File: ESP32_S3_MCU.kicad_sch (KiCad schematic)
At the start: 30 parts, among them SW1 SW_Push, SW2 SW_Push, U1 W25Q32JVSS, U2 ESP32-C3, X1 40MHz

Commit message: Update placement
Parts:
- removed C2: 10u, Capacitor_SMD:C_1210_3225Metric, symbol Device:C_Small
- removed C3, C4, C5, C6: 100n, Capacitor_SMD:C_0603_1608Metric, symbol Device:C_Small
- removed C8: 10u, Capacitor_SMD:C_0603_1608Metric, symbol Device:C_Small
- removed R2, R8: 470R, Resistor_SMD:R_0402_1005Metric, symbol Device:R_Small
- removed R3: 22R, Resistor_SMD:R_0402_1005Metric, symbol Device:R_Small
- removed U2: ESP32-C3, Package_DFN_QFN:QFN-32-1EP_5x5mm_P0.5mm_EP3.45x3.45mm, symbol PCM_Espressif:ESP32-C3
- added C33: 10nF, Capacitor_SMD:C_0402_1005Metric, symbol Device:C_Small
- added C34: 1uF, Capacitor_SMD:C_0402_1005Metric, symbol Device:C_Small
- added C6 (x3), C8: 100n, Capacitor_SMD:C_0402_1005Metric, symbol Device:C_Small
- added C8: 10u, Capacitor_SMD:C_0603_1608Metric, symbol Device:C_Small
- added C8 (x2): 1u, Capacitor_SMD:C_0402_1005Metric, symbol Device:C_Small
- added U8: ESP32-S3, Package_DFN_QFN:QFN-56-1EP_7x7mm_P0.4mm_EP5.6x5.6mm, symbol PCM_Espressif:ESP32-S3
- C1, C11, C12, C21, C22, C7: footprint Capacitor_SMD:C_0603_1608Metric -> Capacitor_SMD:C_0402_1005Metric
- C10, C9: value 10p -> 20p
- L1: footprint Inductor_SMD:L_0603_1608Metric -> Inductor_SMD:L_0402_1005Metric
- U5: footprint RF_Antenna:Texas_SWRA117D_2.4GHz_Right -> RF_Antenna:Texas_SWRA117D_2.4GHz_Left
- X1: footprint Crystal:Crystal_SMD_2520-4Pin_2.5x2.0mm -> KiCADv7:OSC_X322516MLB4SI; Field5 C255973 -> (none); LCSC (none) -> C13738
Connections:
- net +3V3: now also C33.1, C34.1, C6.1, C6.1, C8.1, C8.1, U8.20 (VDD3P3_RTC), U8.46 (VDD3P3_CPU), U8.55 (VDDA), U8.56 (VDDA)
- net CHIP_EN: now also U8.4 (CHIP_PU/RESET)
- net FSPI_CLK: now also U8.44 (MTCK/JTAG/GPIO39)
- net FSPI_D: now also U8.45 (MTDO/JTAG/GPIO40)
- net FSPI_NCS: now also U8.23 (GPIO17/ADC2_CH6)
- net FSPI_NCS2: now also U8.19 (GPIO14/ADC2_CH3)
- net FSPI_Q: now also U8.18 (GPIO13/ADC2_CH2)
- net GND: now also C33.2, C34.2, C6.2, C6.2, C6.2, C8.2, C8.2, C8.2, C8.2, U8.57 (GND)
- net INT_ACC: now also U8.17 (GPIO12/ADC2_CH1)
- net INT_GYR_GPIO9: now also U8.16 (GPIO11/ADC2_CH0); no longer C1.1, R1.2, SW2.2
- net MOTOR_1_DIRECTION: now also U8.7 (GPIO2/ADC1_CH1)
- net MOTOR_1_PWM: now also U8.6 (GPIO1/ADC1_CH0)
- net MOTOR_2_DIRECTION: now also U8.9 (GPIO4/ADC1_CH3)
- net MOTOR_2_PWM: now also U8.8 (GPIO3/ADC1_CH2)
- net RF: now also U8.1 (LNA_IN/RF)
- net SPICLK: now also U8.33 (SPICLK/GPIO30)
- net SPICSO: now also U8.32 (SPICS0/GPIO29)
- net SPID: now also R11.1, U8.35 (SPID/GPIO32)
- net SPIHD: now also U8.30 (SPIHD/GPIO27)
- net SPIQ: now also U8.34 (SPIQ/GPIO31); no longer R11.1
- net SPIWP: now also U8.31 (SPIWP/GPIO28)
- net USB_D_N: now also U8.25 (GPIO19/USB_D-/ADC2_CH8)
- net USB_D_P: now also U8.26 (GPIO20/USB_D+/ADC2_CH9)
- net VDD_SPI: now also C8.1, C8.1, U8.29 (VDD_SPI)
- net V_RF: now also C6.1, U8.2 (VDD3P3), U8.3 (VDD3P3)
- net at C9.1, X1.3: now also U8.53 (XTAL_N)
- net at C10.1, X1.1: now also U8.54 (XTAL_P)
- new net CHIP_BOOT: C1.1, R1.2, SW2.2, U8.5 (GPIO0/BOOT)
- new net MOTOR_3_DIRECTION: U8.11 (GPIO6/ADC1_CH5)
- new net MOTOR_3_PWM: U8.10 (GPIO5/ADC1_CH4)
- new net MOTOR_4_DIRECTION: U8.13 (GPIO8/ADC1_CH7)
- new net MOTOR_4_PWM: U8.12 (GPIO7/ADC1_CH6)
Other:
- moved on the sheet: C12, C13, C21, C22, L1, U1, U5

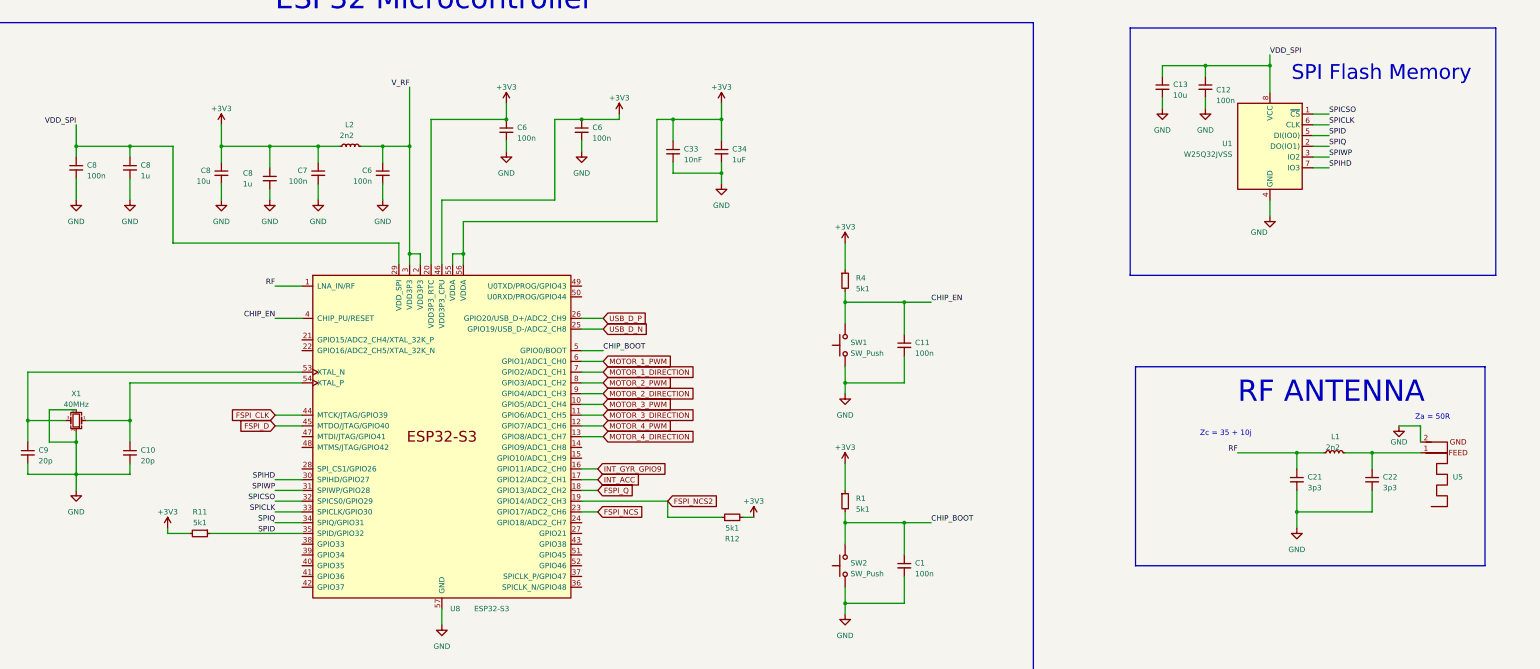
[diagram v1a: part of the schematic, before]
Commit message: route usb and flash
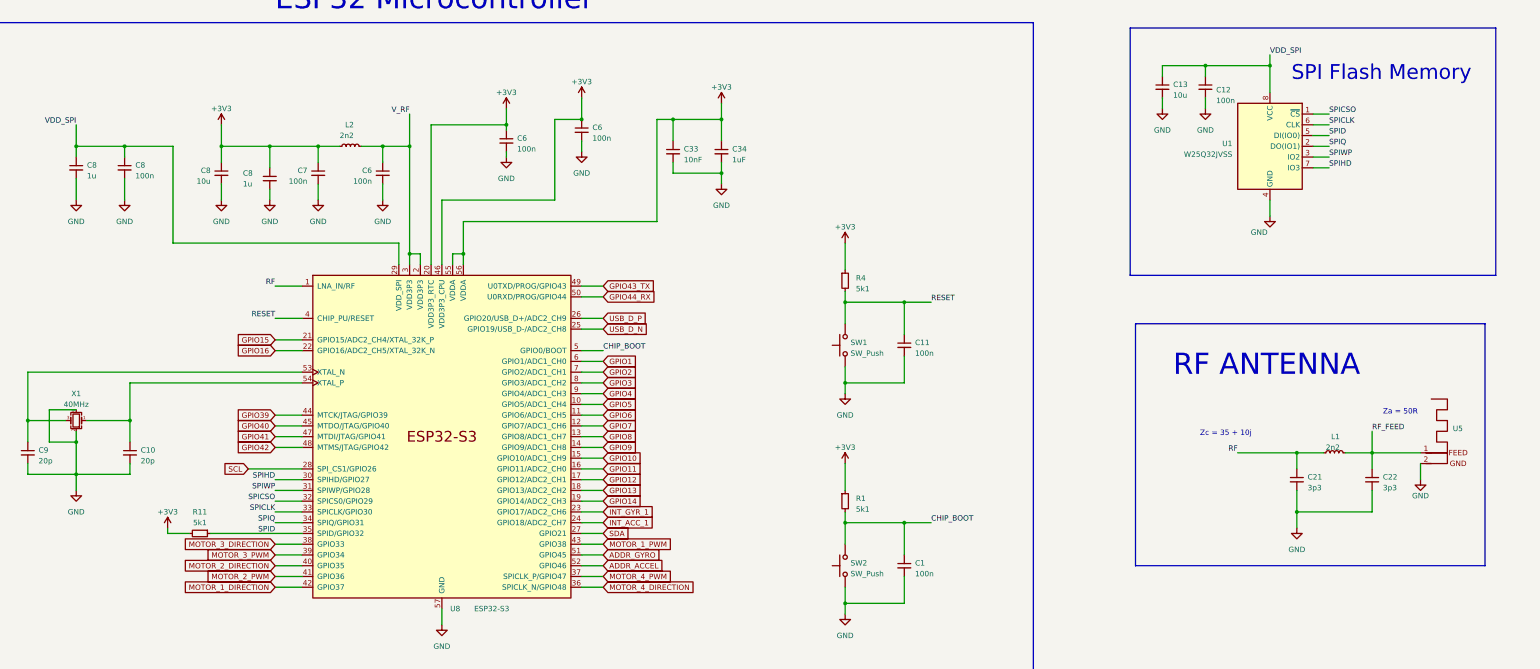
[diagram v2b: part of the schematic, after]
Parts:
- removed R12: 5k1, Resistor_SMD:R_0603_1608Metric, symbol Device:R_Small
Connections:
- net MOTOR_1_DIRECTION: now also U8.42 (GPIO37); no longer U8.7 (GPIO2/ADC1_CH1)
- net MOTOR_1_PWM: now also U8.43 (GPIO38); no longer U8.6 (GPIO1/ADC1_CH0)
- net MOTOR_2_DIRECTION: now also U8.40 (GPIO35); no longer U8.9 (GPIO4/ADC1_CH3)
- net MOTOR_2_PWM: now also U8.41 (GPIO36); no longer U8.8 (GPIO3/ADC1_CH2)
- net MOTOR_3_DIRECTION: now also U8.38 (GPIO33); no longer U8.11 (GPIO6/ADC1_CH5)
- net MOTOR_3_PWM: now also U8.39 (GPIO34); no longer U8.10 (GPIO5/ADC1_CH4)
- net MOTOR_4_DIRECTION: now also U8.36 (SPICLK_N/GPIO48); no longer U8.13 (GPIO8/ADC1_CH7)
- net MOTOR_4_PWM: now also U8.37 (SPICLK_P/GPIO47); no longer U8.12 (GPIO7/ADC1_CH6)
- net RF_FEED: now reaches C22.1, L1.2, U5.1
- net GPIO9: now reaches U8.14 (GPIO9/ADC1_CH8)
- net GPIO10: now reaches U8.15 (GPIO10/ADC1_CH9)
- net GPIO15: now reaches U8.21 (GPIO15/ADC2_CH4/XTAL_32K_P)
- net GPIO16: now reaches U8.22 (GPIO16/ADC2_CH5/XTAL_32K_N)
- net INT_ACC_1: now reaches U8.24 (GPIO18/ADC2_CH7)
- net SDA: now reaches U8.27 (GPIO21)
- net SCL: now reaches U8.28 (SPI_CS1/GPIO26)
- net GPIO41: now reaches U8.47 (MTDI/JTAG/GPIO41)
- net GPIO42: now reaches U8.48 (MTMS/JTAG/GPIO42)
- net GPIO43_TX: now reaches U8.49 (U0TXD/PROG/GPIO43)
- net GPIO44_RX: now reaches U8.50 (U0RXD/PROG/GPIO44)
- net ADDR_GYRO: now reaches U8.51 (GPIO45)
- net ADDR_ACCEL: now reaches U8.52 (GPIO46)
- net CHIP_EN renamed RESET
- net FSPI_CLK renamed GPIO39
- net FSPI_D renamed GPIO40
- net FSPI_NCS renamed INT_GYR_1
- net FSPI_NCS2 renamed GPIO14
- net FSPI_Q renamed GPIO13
- net INT_ACC renamed GPIO12
- net INT_GYR_GPIO9 renamed GPIO11
- new net GPIO1: U8.6 (GPIO1/ADC1_CH0)
- new net GPIO2: U8.7 (GPIO2/ADC1_CH1)
- new net GPIO3: U8.8 (GPIO3/ADC1_CH2)
- new net GPIO4: U8.9 (GPIO4/ADC1_CH3)
- new net GPIO5: U8.10 (GPIO5/ADC1_CH4)
- new net GPIO6: U8.11 (GPIO6/ADC1_CH5)
- new net GPIO7: U8.12 (GPIO7/ADC1_CH6)
- new net GPIO8: U8.13 (GPIO8/ADC1_CH7)
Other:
- moved on the sheet: C6, C8, U5

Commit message: route motors
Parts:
- renumbered C11 to C15, C1 to C16, C13 to C19, C12 to C20, C9 to C23, C8 to C24, C8 to C25, C10 to C26, C8 to C27, C8 to C28, C7 to C29, C6 to C30, C6 to C31, C6 to C32, L1 to L2, L2 to L3, R1 to R10, R11 to R12, R4 to R8, SW1 to SW2, SW2 to SW4, U1 to U6, U5 to U7, X1 to X2

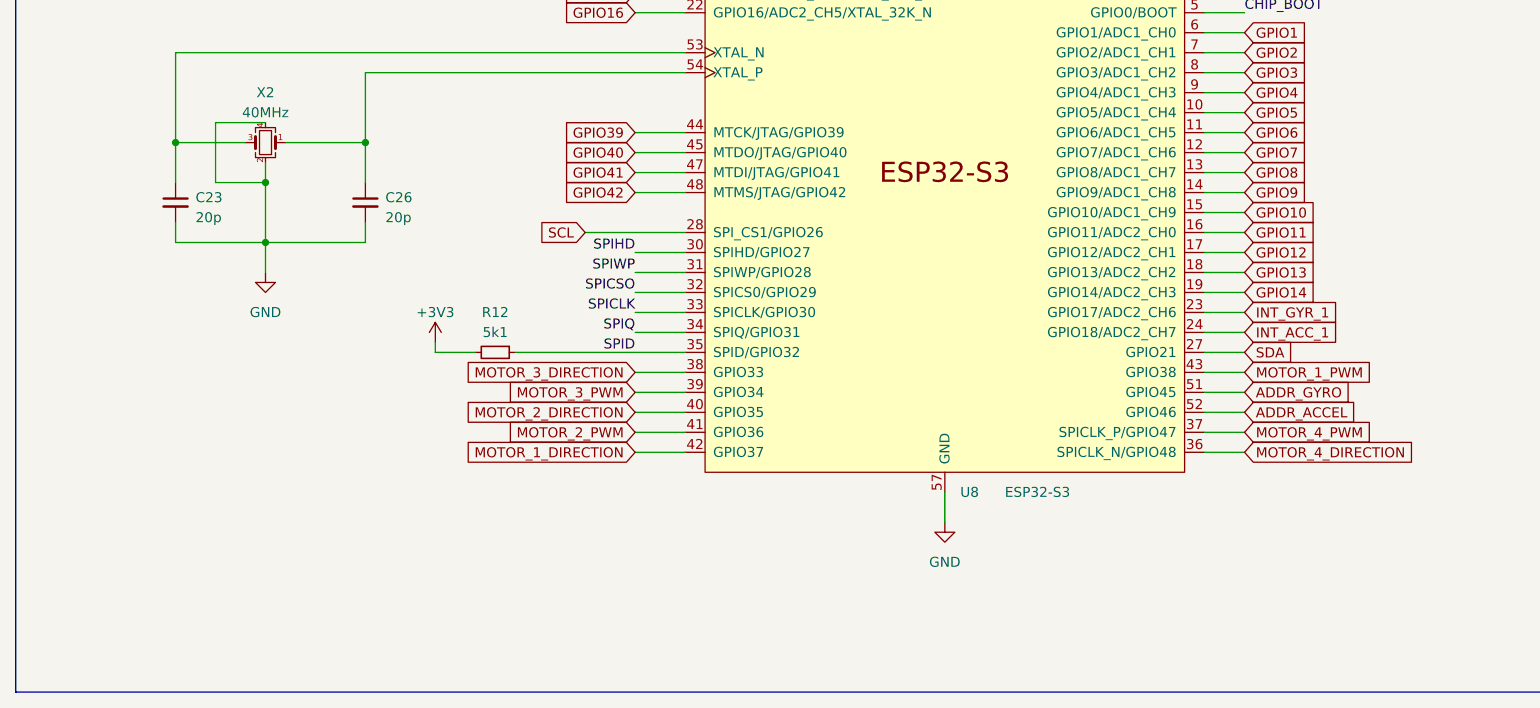
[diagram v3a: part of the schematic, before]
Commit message: Add MPU6050 and LIS2MDL
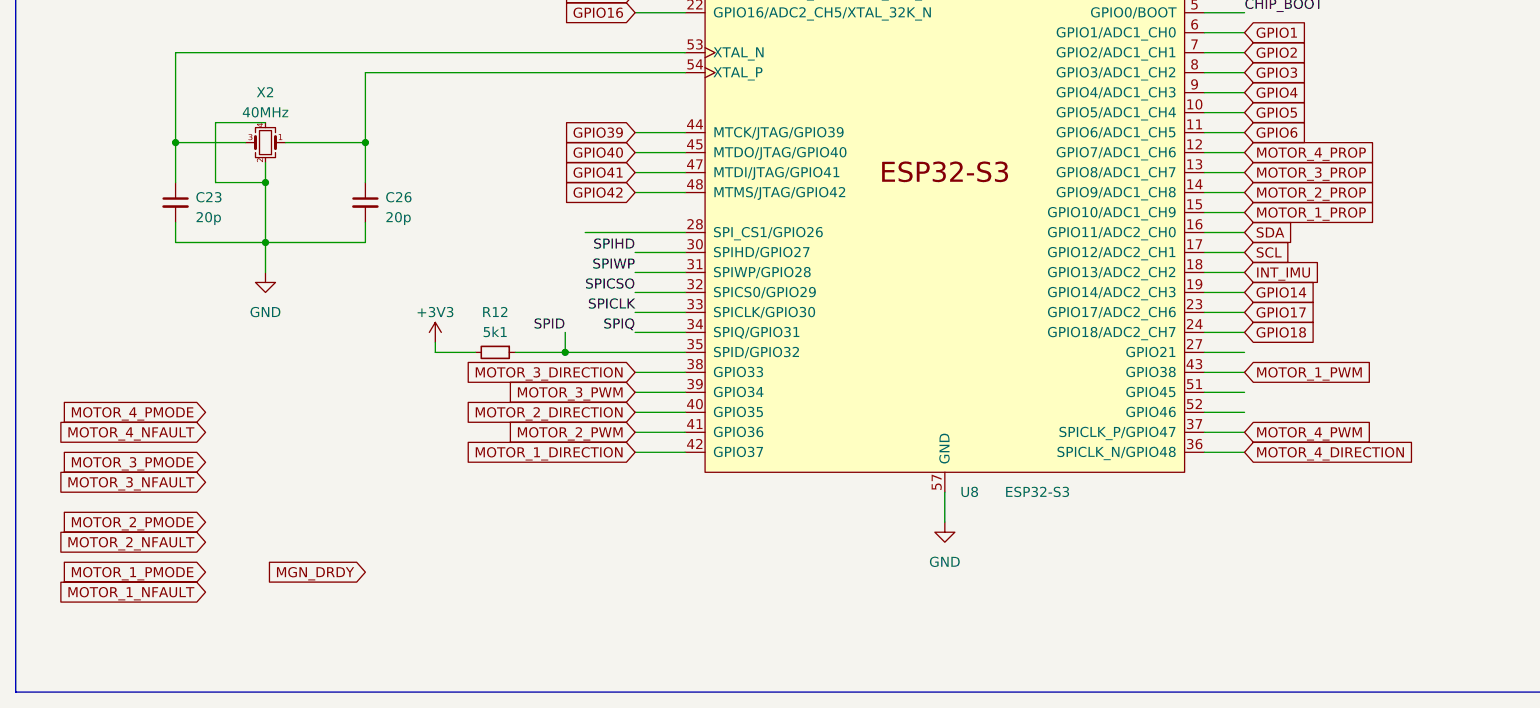
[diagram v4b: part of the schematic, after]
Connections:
- net GPIO11 is gone; now on net SDA: U8.16 (GPIO11/ADC2_CH0)
- net GPIO12 is gone; now on net SCL: U8.17 (GPIO12/ADC2_CH1)
- net SCL: no longer U8.28 (SPI_CS1/GPIO26)
- net SDA: no longer U8.27 (GPIO21)
- net ADDR_ACCEL: no longer names the net of U8.52 (GPIO46)
- net ADDR_GYRO: no longer names the net of U8.51 (GPIO45)
- net GPIO10 renamed MOTOR_1_PROP
- net GPIO13 renamed INT_IMU
- net GPIO7 renamed MOTOR_4_PROP
- net GPIO8 renamed MOTOR_3_PROP
- net GPIO9 renamed MOTOR_2_PROP
- net INT_ACC_1 renamed GPIO18
- net INT_GYR_1 renamed GPIO17

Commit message: checkpoint for backup
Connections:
- net MOTOR_NFAULT: now reaches U8.27 (GPIO21)
- net GPIO26: now reaches U8.28 (SPI_CS1/GPIO26)
- net GPIO45: now reaches U8.51 (GPIO45)
- net GPIO46: now reaches U8.52 (GPIO46)
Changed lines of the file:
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@@
     (stroke (width 0) (type default))
   )
-  (wire (pts (xy 97.79 158.75) (xy 110.49 158.75))
+  (wire (pts (xy 104.14 158.75) (xy 110.49 158.75))
     (stroke (width 0) (type default))
   )
@@
   )
   (wire (pts (xy 194.31 100.33) (xy 194.31 76.2))
+    (stroke (width 0) (type default))
+  )
+  (wire (pts (xy 104.14 157.48) (xy 104.14 158.75))
     (stroke (width 0) (type default))
   )
@@
     )
   )
-  (global_label "MOTOR_4_NFAULT" (shape input) (at 49.53 184.15 180) (fields_autoplaced)
-    (effects (font (size 1.27 1.27)) (justify right))
-    (property "Intersheetrefs" "${INTERSHEET_REFS}" (at 30.2162 184.15 0)
-      (effects (font (size 1.27 1.27)) (justify right) hide)
-    )
-  )
-  (global_label "MOTOR_1_NFAULT" (shape input) (at 49.53 204.47 180) (fields_autoplaced)
-    (effects (font (size 1.27 1.27)) (justify right))
-    (property "Intersheetrefs" "${INTERSHEET_REFS}" (at 30.2162 204.47 0)
-      (effects (font (size 1.27 1.27)) (justify right) hide)
+  (global_label "MOTOR_NFAULT" (shape input) (at 181.61 173.99 0) (fields_autoplaced)
+    (effects (font (size 1.27 1.27)) (justify left))
+    (property "Intersheetrefs" "${INTERSHEET_REFS}" (at 198.7467 173.99 0)
+      (effects (font (size 1.27 1.27)) (justify left) hide)
     )
   )
@@
     )
   )
-  (global_label "MOTOR_2_NFAULT" (shape input) (at 49.53 198.12 180) (fields_autoplaced)
-    (effects (font (size 1.27 1.27)) (justify right))
-    (property "Intersheetrefs" "${INTERSHEET_REFS}" (at 30.2162 198.12 0)
-      (effects (font (size 1.27 1.27)) (justify right) hide)
-    )
-  )
   (global_label "GPIO3" (shape input) (at 181.61 138.43 0) (fields_autoplaced)
     (effects (font (size 1.27 1.27)) (justify left))
@@
     )
   )
+  (global_label "GPIO26" (shape input) (at 104.14 157.48 180) (fields_autoplaced)
+    (effects (font (size 1.27 1.27)) (justify right))
+    (property "Intersheetrefs" "${INTERSHEET_REFS}" (at 94.2605 157.48 0)
+      (effects (font (size 1.27 1.27)) (justify right) hide)
+    )
+  )
   (global_label "MOTOR_2_DIRECTION" (shape input) (at 104.14 181.61 180) (fields_autoplaced)
     (effects (font (size 1.27 1.27)) (justify right))
@@
     )
   )
-  (global_label "MOTOR_2_PMODE" (shape input) (at 49.53 195.58 180) (fields_autoplaced)
-    (effects (font (size 1.27 1.27)) (justify right))
-    (property "Intersheetrefs" "${INTERSHEET_REFS}" (at 30.5792 195.58 0)
-      (effects (font (size 1.27 1.27)) (justify right) hide)
+  (global_label "GPIO46" (shape input) (at 181.61 181.61 0) (fields_autoplaced)
+    (effects (font (size 1.27 1.27)) (justify left))
+    (property "Intersheetrefs" "${INTERSHEET_REFS}" (at 191.4895 181.61 0)
+      (effects (font (size 1.27 1.27)) (justify left) hide)
     )
   )
@@
     )
   )
-  (global_label "MOTOR_1_PMODE" (shape input) (at 49.53 201.93 180) (fields_autoplaced)
-    (effects (font (size 1.27 1.27)) (justify right))
-    (property "Intersheetrefs" "${INTERSHEET_REFS}" (at 30.5792 201.93 0)
-      (effects (font (size 1.27 1.27)) (justify right) hide)
-    )
-  )
-  (global_label "MOTOR_3_NFAULT" (shape input) (at 49.53 190.5 180) (fields_autoplaced)
-    (effects (font (size 1.27 1.27)) (justify right))
-    (property "Intersheetrefs" "${INTERSHEET_REFS}" (at 30.2162 190.5 0)
-      (effects (font (size 1.27 1.27)) (justify right) hide)
-    )
-  )
   (global_label "MOTOR_4_DIRECTION" (shape input) (at 181.61 186.69 0) (fields_autoplaced)
     (effects (font (size 1.27 1.27)) (justify left))
@@
     )
   )
+  (global_label "GPIO45" (shape input) (at 181.61 179.07 0) (fields_autoplaced)
+    (effects (font (size 1.27 1.27)) (justify left))
+    (property "Intersheetrefs" "${INTERSHEET_REFS}" (at 191.4895 179.07 0)
+      (effects (font (size 1.27 1.27)) (justify left) hide)
+    )
+  )
   (global_label "GPIO1" (shape input) (at 181.61 133.35 0) (fields_autoplaced)
     (effects (font (size 1.27 1.27)) (justify left))
@@
     )
   )
-  (global_label "MOTOR_4_PMODE" (shape input) (at 49.53 181.61 180) (fields_autoplaced)
-    (effects (font (size 1.27 1.27)) (justify right))
-    (property "Intersheetrefs" "${INTERSHEET_REFS}" (at 30.5792 181.61 0)
-      (effects (font (size 1.27 1.27)) (justify right) hide)
-    )
-  )
-  (global_label "MOTOR_3_PMODE" (shape input) (at 49.53 187.96 180) (fields_autoplaced)
-    (effects (font (size 1.27 1.27)) (justify right))
-    (property "Intersheetrefs" "${INTERSHEET_REFS}" (at 30.5792 187.96 0)
-      (effects (font (size 1.27 1.27)) (justify right) hide)
-    )
-  )
   (global_label "GPIO40" (shape input) (at 104.14 148.59 180) (fields_autoplaced)
     (effects (font (size 1.27 1.27)) (justify right))
@@
     )
   )
-  (global_label "MGN_DRDY" (shape input) (at 69.85 201.93 180) (fields_autoplaced)
-    (effects (font (size 1.27 1.27)) (justify right))
-    (property "Intersheetrefs" "${INTERSHEET_REFS}" (at 56.9467 201.93 0)
-      (effects (font (size 1.27 1.27)) (justify right) hide)
-    )
-  )

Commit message: Checkpoint before updating MCU
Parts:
- added C10, C54, C57, C9: 100n, Capacitor_SMD:C_0402_1005Metric, symbol Device:C_Small
- added C53: 1u, Capacitor_SMD:C_0402_1005Metric, symbol Device:C_Small
- added C55, C56: 12p, Capacitor_SMD:C_0402_1005Metric, symbol Device:C_Small
- added R21: 10k, symbol Device:R_Small
- added R22, R23: 5k1, Resistor_SMD:R_0603_1608Metric, symbol Device:R_Small
- added SW1, SW3: SW_Push, Button_Switch_SMD:SW_Push_SPST_NO_Alps_SKRK, symbol Switch:SW_Push
- added U4: ESP32-S3-WROOM-1, RF_Module:ESP32-S3-WROOM-1, symbol RF_Module:ESP32-S3-WROOM-1
- added X3: 32.768KHz, Crystal:Crystal_SMD_3225-4Pin_3.2x2.5mm, symbol Device:Crystal_GND24_Small
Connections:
- net +3V3: now also C10.1, C9.1, R21.1, U4.2 (3V3)
- net GND: now also C10.2, C53.2, C54.2, C55.2, C56.2, C57.2, C9.2, SW1.1, SW3.1, U4.1 (GND), U4.40 (GND), U4.41 (GND), X3.2, X3.4
- net USB_D_N: now also U4.13 (IO19)
- net USB_D_P: now also U4.14 (IO20)
- new net: C54.1, R22.2, SW1.2
- new net: C57.1, R23.2, SW3.2
- new net BOOT: R23.1, U4.27 (IO0)
- new net ENABLE: C53.1, R21.2, R22.1, U4.3 (EN)
- new net RXD0: U4.36 (RXD0)
- new net TCK: U4.32 (IO39)
- new net TDI: U4.34 (IO41)
- new net TDO: U4.33 (IO40)
- new net TMS: U4.35 (IO42)
- new net TXD0: U4.37 (TXD0)
- new net XTAL_N: C56.1, U4.9 (IO16), X3.1
- new net XTAL_P: C55.1, U4.8 (IO15), X3.3
